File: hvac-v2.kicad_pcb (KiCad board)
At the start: 2 copper layers, 125 x 93 mm, 138 parts, among them J1 Anderson_two_redblack, J10 Conn_01x02, J11 Conn_01x03, J12 Conn_01x03, J13 Conn_01x03, J14 Conn_01x04, J2 Conn_01x04, J3 Conn_01x02, J4 Anderson_two_redblack_src, J5 Conn_01x03, J6 Conn_01x03, J7 Anderson_two_redblack_sink, J8 Anderson_two_redblack_sink, J9 Conn_01x02, Q1 AO3400A, Q2 AO3400A, Q3 AO3400A, SW1 SW_Push, SW2 Rotary_Encoder_Switch, U1 STM32F030C8Tx, U2 IFX007T, U3 IFX007T, U4 AMS1117-3.3, U5 DS18B20

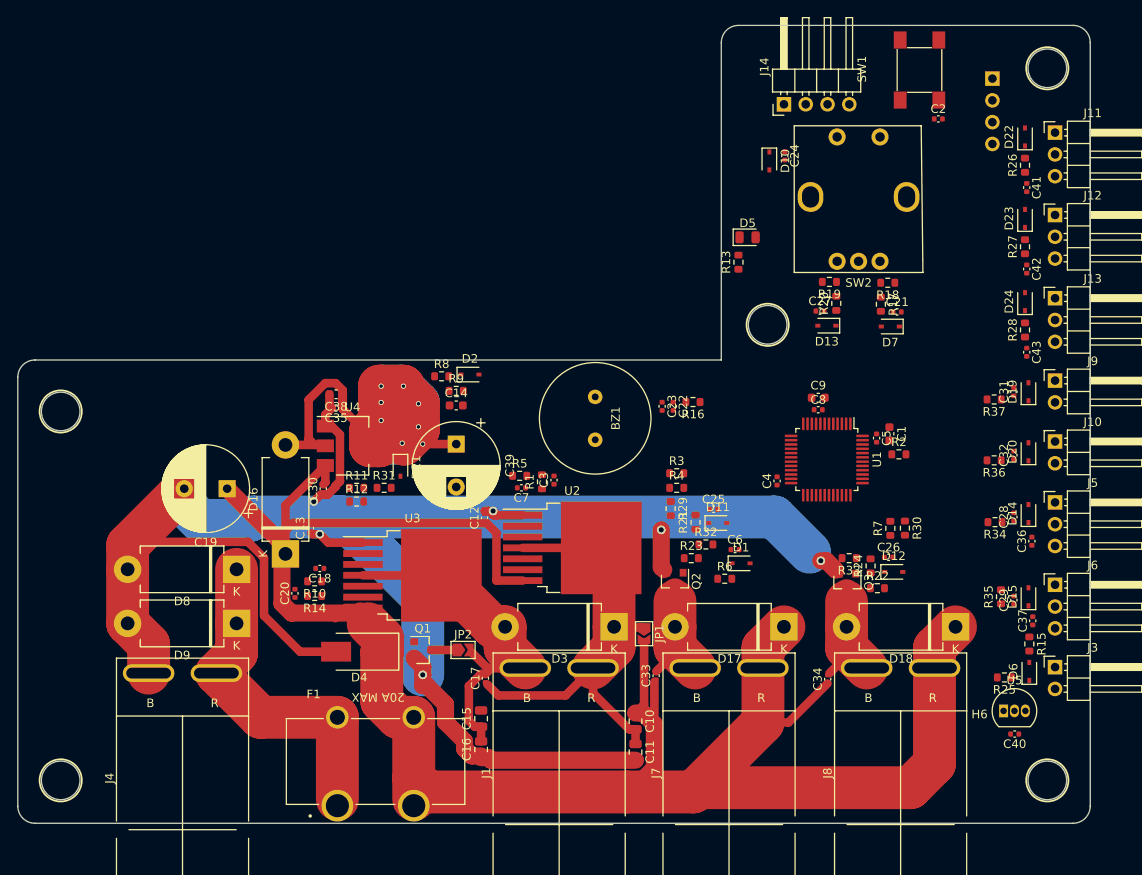
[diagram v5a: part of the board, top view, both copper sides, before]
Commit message: Update to KiCAD v6 format
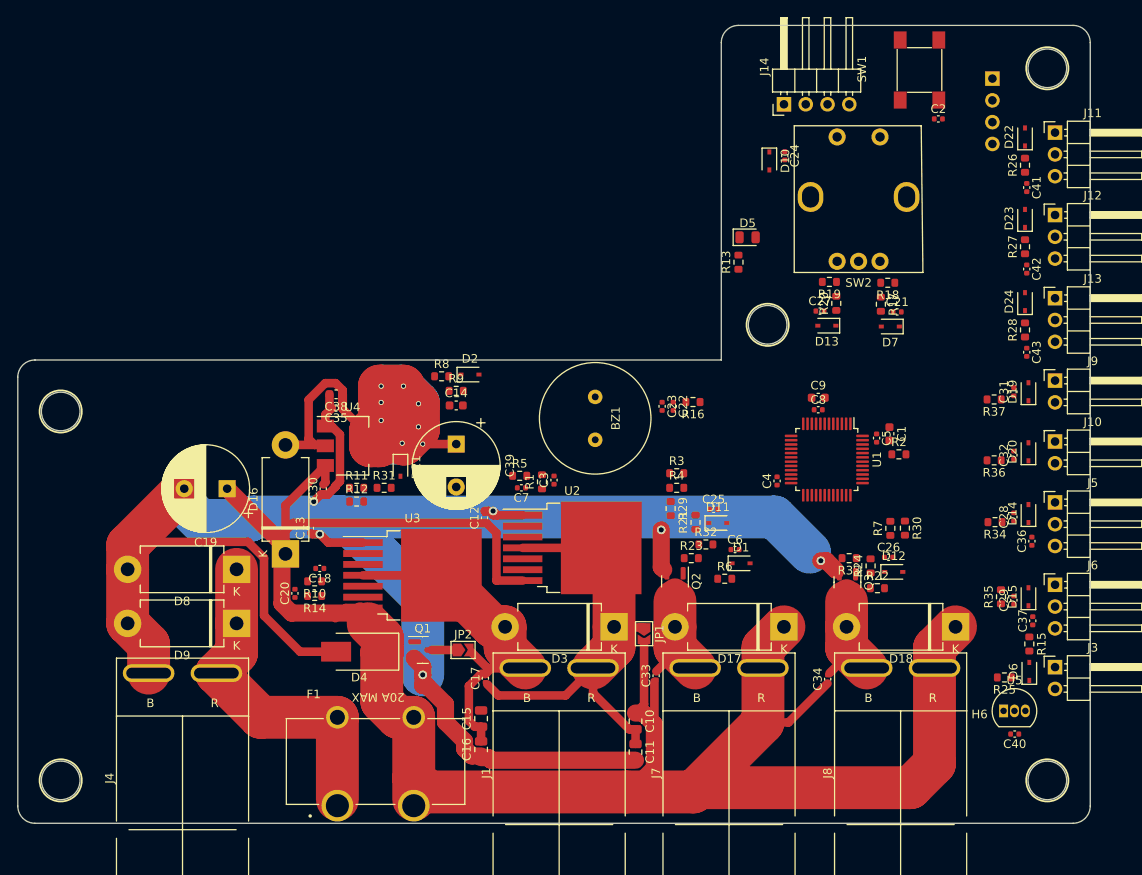
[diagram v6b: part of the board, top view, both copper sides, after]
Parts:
- BZ1: footprint homebrew:MURATA_PKM13EPYH4000-A0 -> Homebrew:MURATA_PKM13EPYH4000-A0
- F1: footprint homebrew:FUSE_3550-2 -> Homebrew:FUSE_3550-2
- H1, H2, H3, H4, H5: footprint homebrew:HOLE_M4 -> Homebrew:HOLE_M4
- H6: footprint homebrew:SLOT_W2mm_H8mm -> Homebrew:SLOT_W2mm_H8mm
- J1, J4, J7, J8: footprint homebrew:Anderson_1336G1_right_angle_bottom_two -> Homebrew:Anderson_1336G1_right_angle_bottom_two
- SW1: footprint homebrew:SW_TACTILE_5.1MM_TS-1187A-C-D-B -> Homebrew:SW_TACTILE_5.1MM_TS-1187A-C-D-B
- SW2: footprint homebrew:BOURNS_PEC12R-4xxxF-Sxxxx -> Homebrew:BOURNS_PEC12R-4xxxF-Sxxxx
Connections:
- U1 pad 2: (no net) -> unconnected-(U1-Pad2)
- U1 pad 3: (no net) -> unconnected-(U1-Pad3)
- U1 pad 33: (no net) -> unconnected-(U1-Pad33)
- U1 pad 35: (no net) -> unconnected-(U1-Pad35)
- U1 pad 36: (no net) -> unconnected-(U1-Pad36)
- U1 pad 38: (no net) -> unconnected-(U1-Pad38)
- U1 pad 4: (no net) -> unconnected-(U1-Pad4)
- U1 pad 40: (no net) -> unconnected-(U1-Pad40)
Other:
- net class Default removed

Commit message: First pass at routing
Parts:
- removed R31: 110k, Resistor_SMD:R_0603_1608Metric
- added C44: 0.1uF, Capacitor_SMD:C_0402_1005Metric, F.Cu at (47.2, 104.8)
- added C45: 0.1uF, Capacitor_SMD:C_0402_1005Metric, F.Cu at (59.5, 100.3)
- added C46: 4.7uF, Capacitor_SMD:C_0603_1608Metric, F.Cu at (58.1, 100.1)
- added D25: D_Schottky, Diode_THT:D_DO-201AD_P12.70mm_Horizontal, F.Cu at (34.7, 124.3)
- added D26: TVS_5V, Diode_SMD:D_SOD-323, F.Cu at (61.2, 100.2)
- added U6: AMS1117-5.0, Package_TO_SOT_SMD:SOT-223-3_TabPin2, F.Cu at (52.6, 102.5)
- moved R7 15.0 mm to (122.7, 129.6)
- moved R30 13.9 mm to (122.7, 126.4), turned to 90 degrees
- moved C13 2.60 mm to (66.7, 117.5)
- moved R4 1.60 mm to (105.2, 112.9), turned to 180 degrees
- turned R3 to 180 degrees
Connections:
- C37 pad 1: VCC -> +5V
- J2 pad 3: VCC -> +5V
- J6 pad 3: VCC -> +5V
- U1 pad 14: /VBATT_DIV -> unconnected-(U1-Pad14)
- U1 pad 15: /PUMP_SENSE -> unconnected-(U1-Pad15)
- U1 pad 25: /SW_2 -> /SW_3
- U1 pad 26: /SW_3 -> /SW_2
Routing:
- net GND: track 232.2 -> 601.7 mm, vias 6 -> 97
- net VCC: track 78.8 -> 326.4 mm, vias 8 -> 14
- net +5V: track 0.00 -> 213.3 mm, vias 0 -> 4
- net /BRIDGE_SENSE_N: track 0.00 -> 123.9 mm, vias 0 -> 2
- net +BATT: track 240.1 -> 316.0 mm, vias 0 -> 3
- net /SWCLK: track 0.00 -> 67.7 mm, vias 0 -> 3
- net /TEMP_INSIDE: track 0.00 -> 64.9 mm, vias 0 -> 3
- net /BRIDGE_ENABLE: track 0.00 -> 59.5 mm, vias 0 -> 3
- net /SWDIO: track 0.00 -> 58.7 mm, vias 0 -> 2
- net /LED: track 0.00 -> 58.3 mm, vias 0 -> 4
- net /TEMP_OUTSIDE: track 0.00 -> 55.7 mm, vias 0 -> 3
- net /NRST: track 0.00 -> 55.3 mm
- net /BRIDGE_N: track 0.00 -> 51.6 mm, vias 0 -> 2
- net /BRIDGE_SENSE_P: track 0.00 -> 49.8 mm, vias 0 -> 4
- net /VBATT_DIV: track 0.00 -> 49.0 mm, vias 0 -> 2
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- added copper zone on B.Cu, net GND
- added copper zone on F.Cu, net GND

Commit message: Hardware revision v2.2.
Complete redesign. Has an I2C port for a screen and a rotary encoder
with a button. Is designed for SMT assembly using JLCPCB.
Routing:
- net /FAN_P: vias 0 -> 7
- net /FAN_N: vias 0 -> 5
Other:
- rule pad_to_mask_clearance: 0.2 -> 0
- board text added: "3V3"
- board text added: "5V"
- board text added: "ACC"
- board text added: "CLK"
- board text added: "FAN"
- board text added: "G"
- board text added: "GND"
- board text added: "IO"
- board text added: "POWER IN"
- board text added: "PUMP"
- board text added: "PWM"
- board text added: "PWM_OUT"
- board text added: "RST"
- board text added: "SCL"
- board text added: "SDA"
- board text added: "SW_1"
- board text added: "SW_2"
- board text added: "SW_3"
- board text added: "SW_WATER"
- board text added: "TEMP_AUX"
- board text added: "TEMP_INSIDE"
- board text added: "TEMP_OUT"
